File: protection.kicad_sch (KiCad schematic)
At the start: 13 parts

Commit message: Weeded out all ERC errors
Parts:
- C1003: renamed from C1201; value 10uF 50V -> 10uF/50V
- C1007: renamed from C1202; value 10uF 50V -> 10uF/50V
- C701: value 100nF 50V -> 100nF/50V
- C702, C703, C704, C705: value 10uF 50V -> 10uF/50V
- F701: footprint (none) -> Hatlabs:Polyfuse_JK60-500
- R701: footprint Capacitor_SMD:C_0603_1608Metric -> Resistor_SMD:R_1206_3216Metric; LCSC (none) -> C25334
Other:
- note added: "FIXME: Replace with LM74700 and N-ch MOSFET"
- company: Hat Labs Ltd -> Hat Labs Oy
- title: Sailor Hat for Raspberry Pi -> HALPI2

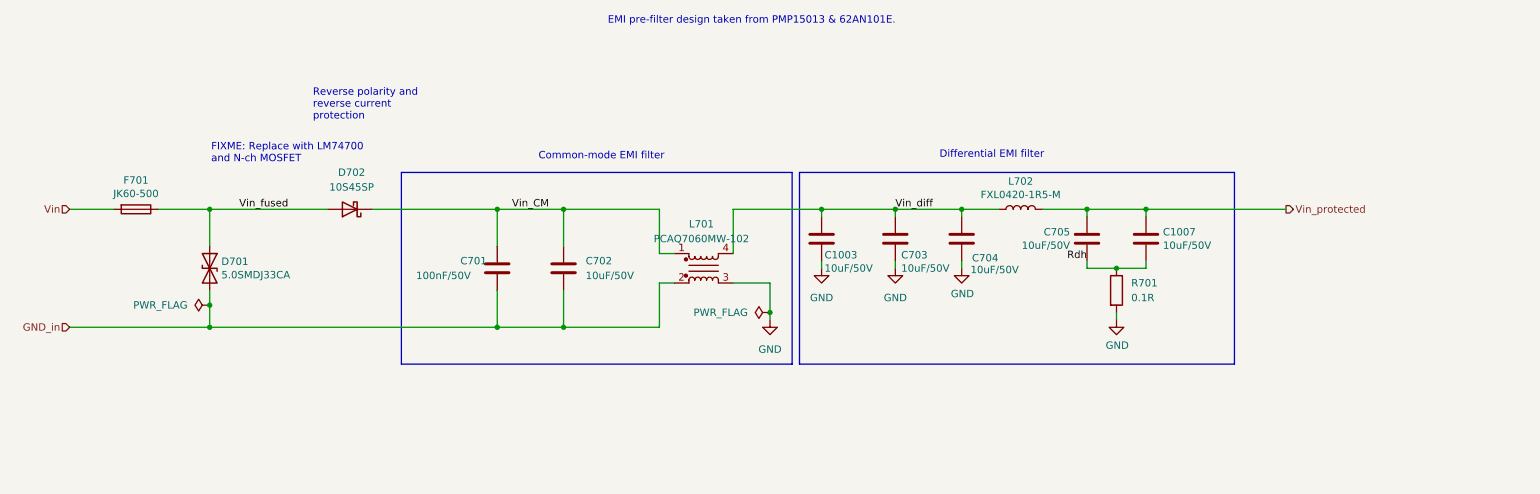
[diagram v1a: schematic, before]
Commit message: Implement ideal diodes for input and LDO power ORing
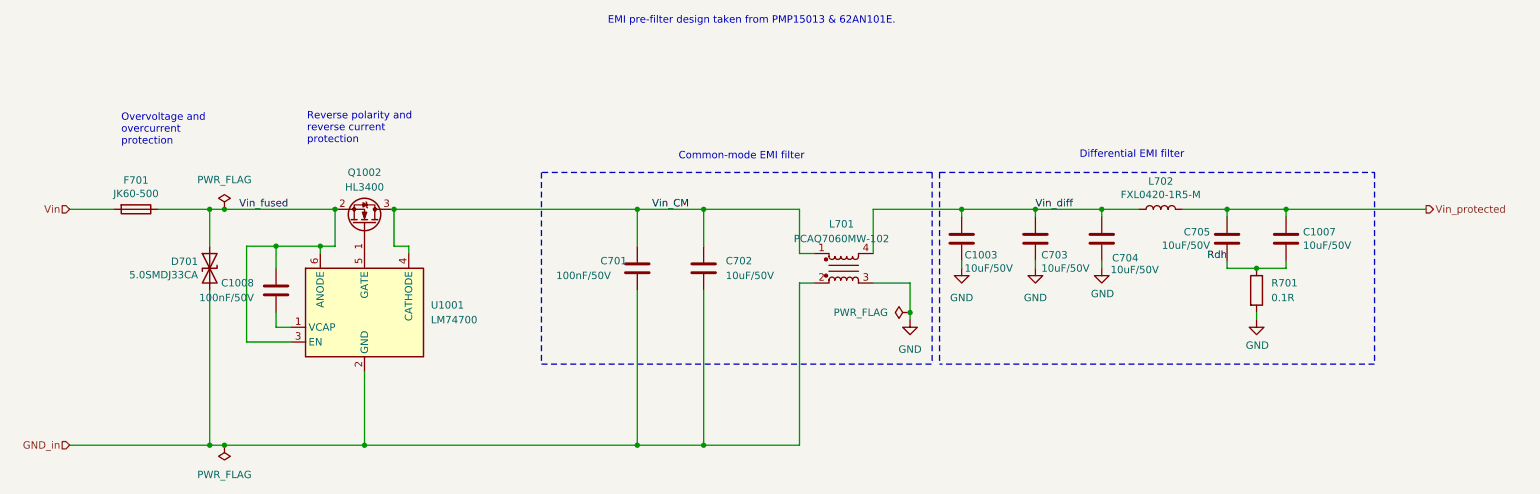
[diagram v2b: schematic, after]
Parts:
- removed D702: 10S45SP, SH-RPi:SS5U100_TO-277, symbol Device:D_Schottky
- added C1008: 100nF/50V, Capacitor_SMD:C_0603_1608Metric, symbol Device:C
- added Q1002: HL3400, Package_TO_SOT_SMD:SOT-23, symbol Hatlabs:HL3400
- added U1001: LM74700, Package_TO_SOT_SMD:SOT-23-6, symbol Power_Management:LM74700
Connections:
- net GND_in: now also U1001.2 (GND)
- net Vin_CM: now also Q1002.3 (D), U1001.4 (CATHODE)
- net Vin_fused: now also C1008.1, Q1002.2 (S), U1001.3 (EN), U1001.6 (ANODE)
- new net: C1008.2, U1001.1 (VCAP)
- new net: Q1002.1 (G), U1001.5 (GATE)
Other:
- note added: "Overvoltage and overcurrent protection"
- note removed: "FIXME: Replace with LM74700 and N-ch MOSFET"
- moved on the sheet: C1003, C1007, C701, C702, C703, C704, C705, D701, L701, L702, R701

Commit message: Re-annotate schematics
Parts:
- renumbered C1008 to C1001, C1003 to C1004, C1007 to C1008, Q1002 to Q1001
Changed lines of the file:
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@@
-			)
-		)
-		(property "Sim.Enable" ""
-			(at 55.88 63.5 0)
-			(effects
-				(font
-					(size 1.27 1.27)
-				)
-				(hide yes)
 			)
 		)
@@
 			)
 		)
-		(property "Sim.Enable" ""
-			(at 43.18 53.34 0)
-			(effects
-				(font
-					(size 1.27 1.27)
-				)
-				(hide yes)
-			)
-		)
 		(pin "1"
 		)
@@
 			)
 		)
-		(property "Sim.Enable" ""
-			(at 209.55 58.42 0)
-			(effects
-				(font
-					(size 1.27 1.27)
-				)
-				(hide yes)
-			)
-		)
 		(pin "1"
 		)
@@
 			(project "SH-RPi"
 				(path "/abc482bd-3f17-4d35-80db-1da3dcdb5c27/c7bf4e1f-6bd1-4be7-9e56-1bd438bf5d42/b9ac802e-51d9-4be8-a7d3-5b5fa2c8bb97"
-					(reference "C1005")
+					(reference "C1006")
 					(unit 1)
 				)
@@
 		(property "LCSC" "C167205"
 			(at 219.71 53.34 90)
-			(effects
-				(font
-					(size 1.27 1.27)
-				)
-				(hide yes)
-			)
-		)
-		(property "Sim.Enable" ""
-			(at 219.71 53.34 0)
 			(effects
 				(font
@@
 			)
 		)
-		(property "Sim.Enable" ""
-			(at 231.14 58.42 0)
-			(effects
-				(font
-					(size 1.27 1.27)
-				)
-				(hide yes)
-			)
-		)
 		(pin "1"
 		)
@@
 			(project "SH-RPi"
 				(path "/abc482bd-3f17-4d35-80db-1da3dcdb5c27/c7bf4e1f-6bd1-4be7-9e56-1bd438bf5d42/b9ac802e-51d9-4be8-a7d3-5b5fa2c8bb97"
-					(reference "C1006")
+					(reference "C1007")
 					(unit 1)
 				)
@@
 			)
 		)
-		(property "Sim.Enable" ""
-			(at 236.22 67.31 0)
-			(effects
-				(font
-					(size 1.27 1.27)
-				)
-				(hide yes)
-			)
-		)
 		(pin "1"
 		)
@@
 		(on_board yes)
 		(dnp no)
-		(property "Reference" "C1007"
+		(property "Reference" "C1008"
 			(at 244.221 57.2516 0)
 			(effects
@@
 			)
 		)
-		(property "Sim.Enable" ""
-			(at 241.3 58.42 0)
-			(effects
-				(font
-					(size 1.27 1.27)
-				)
-				(hide yes)
-			)
-		)
 		(pin "1"
 		)
@@
 			(project "Yellow"
 				(path "/abc482bd-3f17-4d35-80db-1da3dcdb5c27/c7bf4e1f-6bd1-4be7-9e56-1bd438bf5d42/b9ac802e-51d9-4be8-a7d3-5b5fa2c8bb97"
-					(reference "C1007")
+					(reference "C1008")
 					(unit 1)
 				)
@@
 			(project "SH-RPi"
 				(path "/abc482bd-3f17-4d35-80db-1da3dcdb5c27/c7bf4e1f-6bd1-4be7-9e56-1bd438bf5d42/b9ac802e-51d9-4be8-a7d3-5b5fa2c8bb97"
-					(reference "#FLG01001")
+					(reference "#FLG01002")
 					(unit 1)
 				)
@@
 			)
 		)
-		(property "Sim.Enable" ""
-			(at 140.97 63.5 0)
-			(effects
-				(font
-					(size 1.27 1.27)
-				)
-				(hide yes)
-			)
-		)
 		(pin "1"
 		)
@@
 			(project "SH-RPi"
 				(path "/abc482bd-3f17-4d35-80db-1da3dcdb5c27/c7bf4e1f-6bd1-4be7-9e56-1bd438bf5d42/b9ac802e-51d9-4be8-a7d3-5b5fa2c8bb97"
-					(reference "C1002")
+					(reference "C1003")
 					(unit 1)
 				)
@@
 		(on_board yes)
 		(dnp no)
-		(property "Reference" "C1003"
+		(property "Reference" "C1004"
 			(at 185.928 61.214 0)
 			(effects
@@
 			)
 		)
-		(property "Sim.Enable" ""
-			(at 185.42 58.42 0)
-			(effects
-				(font
-					(size 1.27 1.27)
-				)
-				(hide yes)
-			)
-		)
 		(pin "1"
 		)
@@
 			(project "Yellow"
 				(path "/abc482bd-3f17-4d35-80db-1da3dcdb5c27/c7bf4e1f-6bd1-4be7-9e56-1bd438bf5d42/b9ac802e-51d9-4be8-a7d3-5b5fa2c8bb97"
-					(reference "C1003")
+					(reference "C1004")
 					(unit 1)
 				)
@@
 			)
 		)
-		(property "Sim.Enable" ""
-			(at 198.12 58.42 0)
-			(effects
-				(font
-					(size 1.27 1.27)
-				)
-				(hide yes)
-			)
-		)
 		(pin "1"
 		)
@@
 			(project "SH-RPi"
 				(path "/abc482bd-3f17-4d35-80db-1da3dcdb5c27/c7bf4e1f-6bd1-4be7-9e56-1bd438bf5d42/b9ac802e-51d9-4be8-a7d3-5b5fa2c8bb97"
-					(reference "C1004")
+					(reference "C1005")
 					(unit 1)
 				)
@@
 			)
 		)
-		(property "Sim.Enable" ""
-			(at 129.54 63.5 0)
-			(effects
-				(font
-					(size 1.27 1.27)
-				)
-				(hide yes)
-			)
-		)
 		(pin "1"
 		)
@@
 			(project "SH-RPi"
 				(path "/abc482bd-3f17-4d35-80db-1da3dcdb5c27/c7bf4e1f-6bd1-4be7-9e56-1bd438bf5d42/b9ac802e-51d9-4be8-a7d3-5b5fa2c8bb97"
-					(reference "C1001")
+					(reference "C1002")
 					(unit 1)
 				)
@@
 		(dnp no)
 		(fields_autoplaced yes)
-		(property "Reference" "#FLG01003"
+		(property "Reference" "#FLG01001"
 			(at 58.42 51.435 0)
 			(effects
@@
 			(project "HALPI2"
 				(path "/abc482bd-3f17-4d35-80db-1da3dcdb5c27/c7bf4e1f-6bd1-4be7-9e56-1bd438bf5d42/b9ac802e-51d9-4be8-a7d3-5b5fa2c8bb97"
-					(reference "#FLG01003")
+					(reference "#FLG01001")
 					(unit 1)
 				)
@@
 			)
 		)
-		(property "Sim.Enable" ""
-			(at 165.1 63.5 0)
-			(effects
-				(font
-					(size 1.27 1.27)
-				)
-				(hide yes)
-			)
-		)
 		(pin "1"
 		)
@@
 		(dnp no)
 		(fields_autoplaced yes)
-		(property "Reference" "Q1002"
+		(property "Reference" "Q1001"
 			(at 82.55 46.99 90)
 			(effects
@@
 			(project ""
 				(path "/abc482bd-3f17-4d35-80db-1da3dcdb5c27/c7bf4e1f-6bd1-4be7-9e56-1bd438bf5d42/b9ac802e-51d9-4be8-a7d3-5b5fa2c8bb97"
-					(reference "Q1002")
+					(reference "Q1001")
 					(unit 1)
 				)
@@
 		(dnp no)
 		(fields_autoplaced yes)
-		(property "Reference" "#FLG01002"
+		(property "Reference" "#FLG01003"
 			(at 174.625 71.12 0)
 			(effects
@@
 			(project "HALPI2"
 				(path "/abc482bd-3f17-4d35-80db-1da3dcdb5c27/c7bf4e1f-6bd1-4be7-9e56-1bd438bf5d42/b9ac802e-51d9-4be8-a7d3-5b5fa2c8bb97"
-					(reference "#FLG01002")
+					(reference "#FLG01003")
 					(unit 1)
 				)
@@
 		(on_board yes)
 		(dnp no)
-		(property "Reference" "C1008"
+		(property "Reference" "C1001"
 			(at 63.5 66.0399 0)
 			(effects
@@
 			(project "HALPI2"
 				(path "/abc482bd-3f17-4d35-80db-1da3dcdb5c27/c7bf4e1f-6bd1-4be7-9e56-1bd438bf5d42/b9ac802e-51d9-4be8-a7d3-5b5fa2c8bb97"
-					(reference "C1008")
-					(unit 1)
-				)
+					(reference "C1001")
+					(unit 1)
+				)

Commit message: Fix ethernet port & other changes
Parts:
- L701: footprint SH-RPi:L_CMF7060F -> Hatlabs:L_CMF7060F
- L702: footprint SH-RPi:L_MWSA0402 -> Hatlabs:L_MWSA0402
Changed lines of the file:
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@@
 			)
 		)
-		(property "Footprint" "SH-RPi:L_MWSA0402"
+		(property "Footprint" "Hatlabs:L_MWSA0402"
 			(at 219.71 53.34 0)
 			(effects
@@
 			)
 		)
-		(property "Footprint" "SH-RPi:L_CMF7060F"
+		(property "Footprint" "Hatlabs:L_CMF7060F"
 			(at 165.1 63.5 0)
 			(effects

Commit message: Finish component selection for USB3 hub
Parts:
- U1001: LCSC (none) -> C2941042
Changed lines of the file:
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@@
+			)
+		)
+		(property "LCSC" "C2941042"
+			(at 82.55 71.12 0)
+			(effects
+				(font
+					(size 1.27 1.27)
+				)
+				(hide yes)
 			)
 		)

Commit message: Partial trace layout, kick-ass custom rules
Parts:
- renumbered C1004 to C1201, C1008 to C1205, C1001 to C1208, Q1001 to Q1201, U1001 to U1201
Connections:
- net VCAP: now reaches C1208.2, U1201.1 (VCAP)
- net G: now reaches Q1201.1 (G), U1201.5 (GATE)
